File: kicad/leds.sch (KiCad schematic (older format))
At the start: 85 parts, among them U6 74HC154

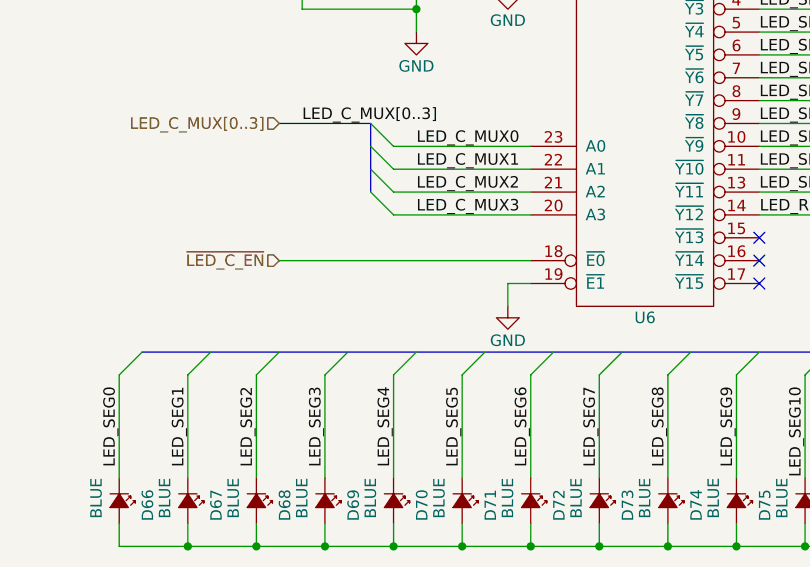
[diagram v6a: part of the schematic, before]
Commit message: Finished round two routing
This layout cuts through the middle of no planes and has more
predictable power paths (without needing Hyperlynx or something like
that). It also routes all signals but the LED-related ones on just the
top and bottom layers, as it is meant to be. It also nearly comforms to
the recommended layout for the regulator. There also aren't any ICs
without a full reference plane beneath them.

Basically, it's awesome.
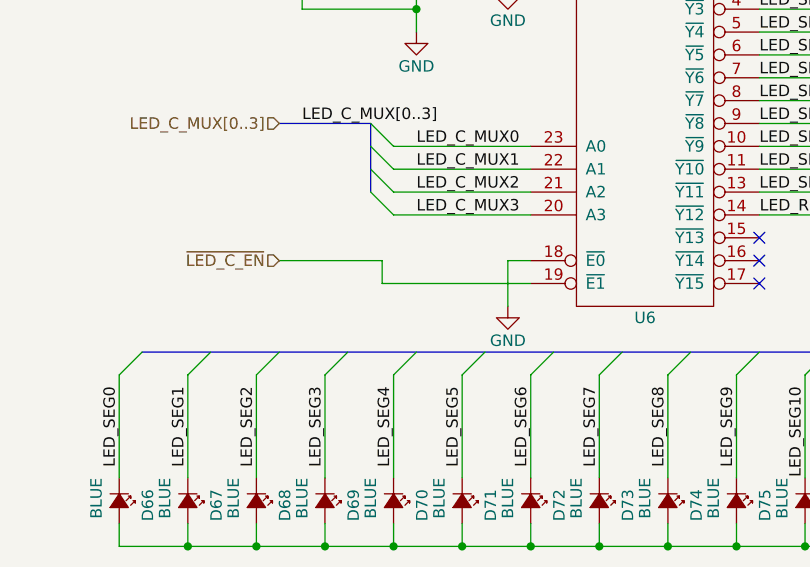
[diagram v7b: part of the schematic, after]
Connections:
- net GND: now also U6.18 (~E0); no longer U6.19 (~E1)
- net ~LED_C_EN: now also U6.19 (~E1); no longer U6.18 (~E0)
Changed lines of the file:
@@
 Text Label 4100 6200 2    50   ~ 0
 LED_RGB_C
-Wire Wire Line
-	1600 6400 2700 6400
 Wire Bus Line
 	1600 5800 2000 5800
@@
 	1700 5300 2200 5300
 Connection ~ 2200 5300
-Wire Wire Line
-	2600 6600 2600 6500
-Wire Wire Line
-	2600 6500 2700 6500
 Wire Wire Line
 	4600 1300 4600 1400
@@
 	1    0    0    -1
 $EndComp
+Wire Wire Line
+	2700 6400 2600 6400
+Wire Wire Line
+	2600 6400 2600 6600
+Wire Wire Line
+	2050 6500 2700 6500
+Wire Wire Line
+	2050 6500 2050 6400
+Wire Wire Line
+	2050 6400 1600 6400
 $EndSCHEMATC

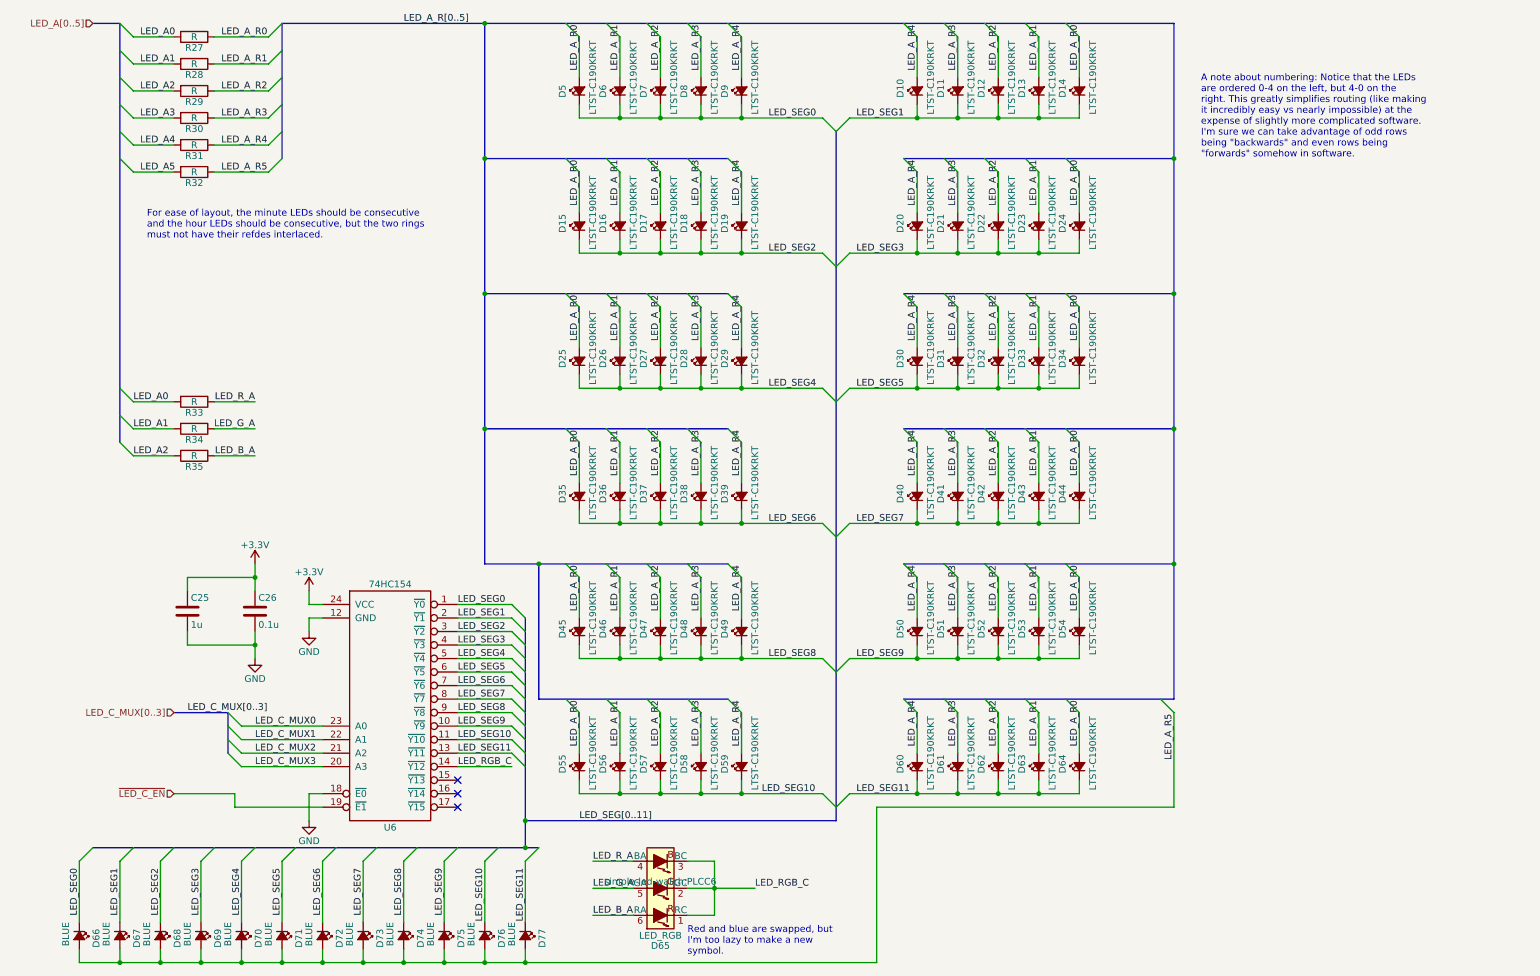
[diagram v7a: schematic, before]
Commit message: Changed out D65 RGB LED for a shorter 0606 part
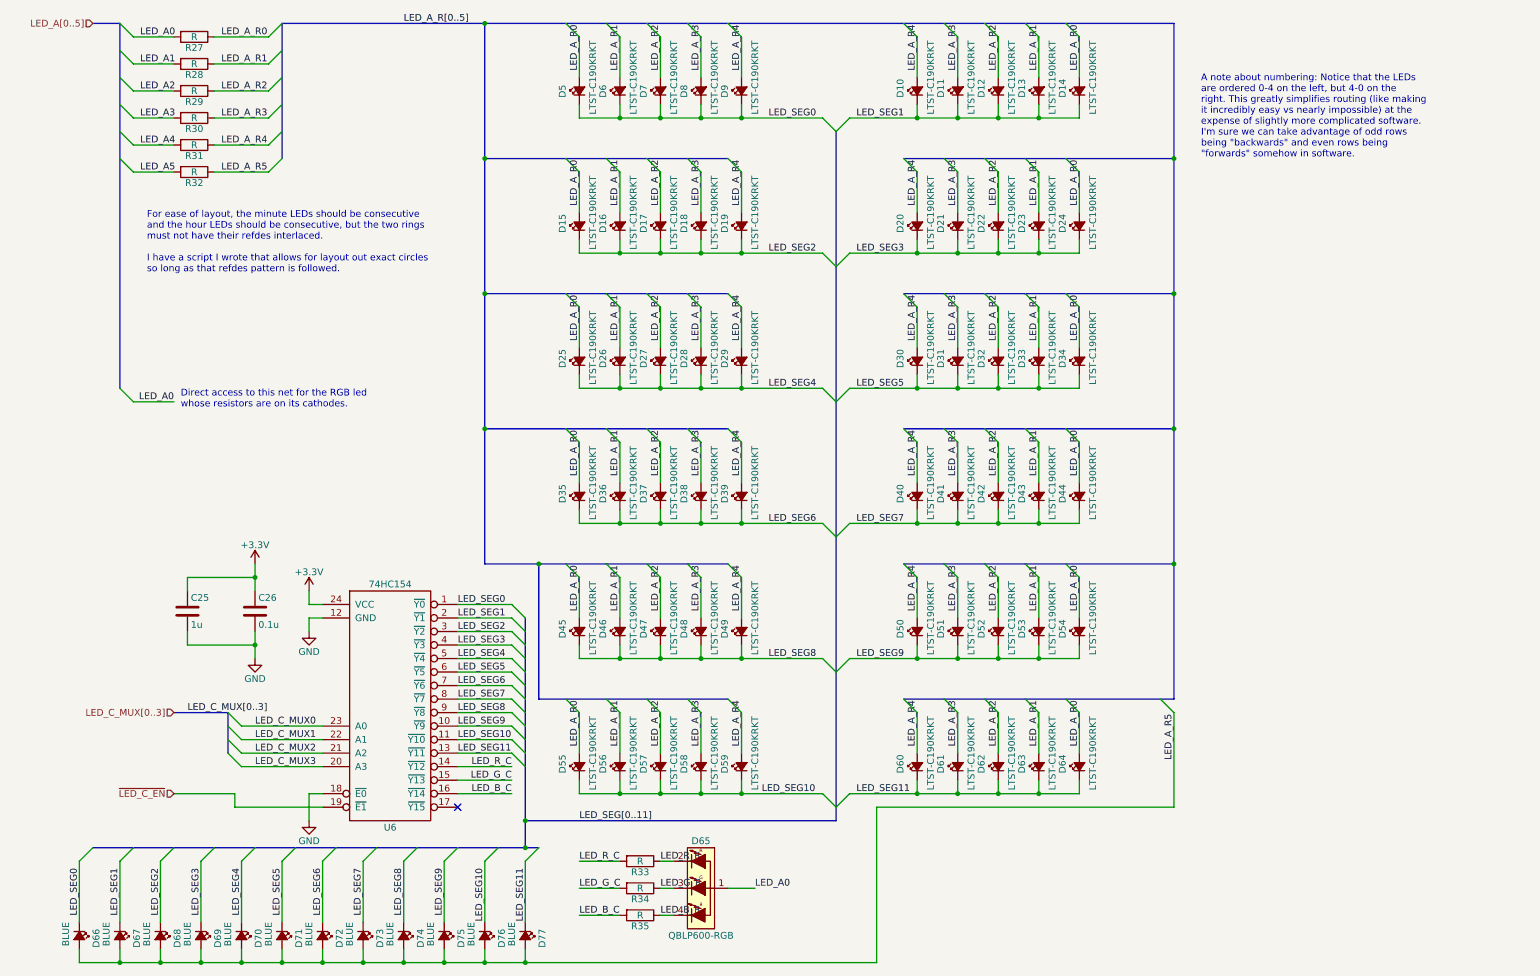
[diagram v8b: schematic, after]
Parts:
- removed D65: LED_RGB, simple-led-watch:PLCC6, symbol LED_RGB
- added D65: QBLP600-RGB, simple-led-watch:LED-0606, symbol Led_RGB_CA
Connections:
- net LED_A0: now also D65.1; no longer R33.2
- net LED_A1: no longer R34.2
- net LED_A2: no longer R35.2
- net LED_G_C: now reaches U6.15 (~Y13)
- net LED_G_C: now also R34.2
- net LED_B_C: now reaches U6.16 (~Y14)
- net LED_B_C: now also R35.2
- net LED_B_A renamed LED_B_R
- net LED_B_R: now also D65.4 (B)
- net LED_G_A renamed LED_G_R
- net LED_G_R: now also D65.3 (G)
- net LED_RGB_C renamed LED_R_C
- net LED_R_C: now also R33.2
- net LED_R_A renamed LED_R_R
- net LED_R_R: now also D65.2 (R)
- no-connect marks 3 -> 1
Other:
- note added: "Direct access to this net for the RGB led\nwhose resistors are on its cathodes."
- note added: "For ease of layout, the minute LEDs should be consecutive\nand the hour LEDs should be consecutive, but the two rings\nmust not have their refdes interlaced.\n\nI have a script I wrote that allows for layout out exact circles\nso long as that refdes pattern is followed."
- note removed: "For ease of layout, the minute LEDs should be consecutive\nand the hour LEDs should be consecutive, but the two rings\nmust not have their refdes interlaced."
- note removed: "Red and blue are swapped, but\nI'm too lazy to make a new\nsymbol."
- moved on the sheet: R33, R34, R35
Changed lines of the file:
@@
 Entry Wire Line
 	4200 6900 4300 6800
-Text Notes 1400 2300 0    50   ~ 0
-For ease of layout, the minute LEDs should be consecutive\nand the hour LEDs should be consecutive, but the two rings\nmust not have their refdes interlaced.
+Text Notes 1400 2550 0    50   ~ 0
+For ease of layout, the minute LEDs should be consecutive\nand the hour LEDs should be consecutive, but the two rings\nmust not have their refdes interlaced.\n\nI have a script I wrote that allows for layout out exact circles\nso long as that refdes pattern is followed.
 Entry Wire Line
 	8900 5700 9000 5800
@@
 Text Label 6650 6400 0    50   ~ 0
 LED_SEG11
-Text Label 4100 6200 2    50   ~ 0
-LED_RGB_C
 Wire Bus Line
 	1600 5800 2000 5800
@@
 	1000 700  1200 700
 Wire Bus Line
-	1200 700  1200 3800
-Wire Bus Line
 	2400 700  2400 1700
 Wire Wire Line
@@
 	9000 6500 6800 6500
 Connection ~ 4200 7650
-Wire Wire Line
-	3700 6200 4100 6200
-$Comp
-L LED_RGB D65
-U 1 1 5804CA95
-P 5200 7100
-F 0 "D65" H 5200 7525 50  0000 C CNN
-F 1 "LED_RGB" H 5200 7450 50  0000 C CNN
-F 2 "simple-led-watch:PLCC6" H 5200 7050 50  0000 C CNN
-F 3 "" H 5200 7050 50  0000 C CNN
-F 4 "CLY6D-FKC-CNP1ST1E1BB7D3D3CT-ND" H 5200 7100 60  0001 C CNN "Part No."
-	1    5200 7100
-	-1   0    0    1
-$EndComp
-Text Notes 5400 7600 0    50   ~ 0
-Red and blue are swapped, but\nI'm too lazy to make a new\nsymbol.
 $Comp
 L R R33
 U 1 1 5804E18D
-P 1750 3500
-F 0 "R33" V 1830 3500 50  0000 C CNN
-F 1 "R" V 1750 3500 50  0000 C CNN
-F 2 "Resistors_SMD:R_0402" V 1680 3500 50  0001 C CNN
-F 3 "" H 1750 3500 50  0000 C CNN
-	1    1750 3500
+P 5050 6900
+F 0 "R33" V 5130 6900 50  0000 C CNN
+F 1 "R" V 5050 6900 50  0000 C CNN
+F 2 "Resistors_SMD:R_0402" V 4980 6900 50  0001 C CNN
+F 3 "" H 5050 6900 50  0000 C CNN
+	1    5050 6900
 	0    1    1    0
 $EndComp
@@
 L R R34
 U 1 1 5804E381
-P 1750 3700
-F 0 "R34" V 1830 3700 50  0000 C CNN
-F 1 "R" V 1750 3700 50  0000 C CNN
-F 2 "Resistors_SMD:R_0402" V 1680 3700 50  0001 C CNN
-F 3 "" H 1750 3700 50  0000 C CNN
-	1    1750 3700
+P 5050 7100
+F 0 "R34" V 5130 7100 50  0000 C CNN
+F 1 "R" V 5050 7100 50  0000 C CNN
+F 2 "Resistors_SMD:R_0402" V 4980 7100 50  0001 C CNN
+F 3 "" H 5050 7100 50  0000 C CNN
+	1    5050 7100
 	0    1    1    0
 $EndComp
@@
 L R R35
 U 1 1 5804E495
-P 1750 3900
-F 0 "R35" V 1830 3900 50  0000 C CNN
-F 1 "R" V 1750 3900 50  0000 C CNN
-F 2 "Resistors_SMD:R_0402" V 1680 3900 50  0001 C CNN
-F 3 "" H 1750 3900 50  0000 C CNN
-	1    1750 3900
+P 5050 7300
+F 0 "R35" V 5130 7300 50  0000 C CNN
+F 1 "R" V 5050 7300 50  0000 C CNN
+F 2 "Resistors_SMD:R_0402" V 4980 7300 50  0001 C CNN
+F 3 "" H 5050 7300 50  0000 C CNN
+	1    5050 7300
 	0    1    1    0
 $EndComp
 Text Label 5900 7100 0    50   ~ 0
-LED_RGB_C
-Wire Wire Line
-	5400 7100 5900 7100
-Wire Wire Line
-	5600 6900 5600 7300
-Wire Wire Line
-	5600 6900 5400 6900
-Connection ~ 5600 7100
-Wire Wire Line
-	5600 7300 5400 7300
-Wire Wire Line
-	1900 3500 2200 3500
-Wire Wire Line
-	1900 3700 2200 3700
-Wire Wire Line
-	1900 3900 2200 3900
-Text Label 2200 3500 2    50   ~ 0
-LED_R_A
-Text Label 2200 3700 2    50   ~ 0
-LED_G_A
-Text Label 2200 3900 2    50   ~ 0
-LED_B_A
-Entry Wire Line
-	1200 3800 1300 3900
-Entry Wire Line
-	1200 3600 1300 3700
+LED_A0
 Entry Wire Line
 	1200 3400 1300 3500
 Wire Wire Line
 	1300 3500 1600 3500
-Wire Wire Line
-	1300 3700 1600 3700
-Wire Wire Line
-	1300 3900 1600 3900
-Text Label 1300 3500 0    50   ~ 0
+Text Label 1600 3500 2    50   ~ 0
 LED_A0
-Text Label 1300 3700 0    50   ~ 0
-LED_A1
-Text Label 1300 3900 0    50   ~ 0
-LED_A2
 Connection ~ 4200 6800
 Wire Wire Line
 	6800 6500 6800 7650
-Wire Wire Line
-	4700 6900 5000 6900
-Wire Wire Line
-	4700 7100 5000 7100
-Wire Wire Line
-	4700 7300 5000 7300
-Text Label 4700 6900 0    50   ~ 0
-LED_R_A
-Text Label 4700 7100 0    50   ~ 0
-LED_G_A
-Text Label 4700 7300 0    50   ~ 0
-LED_B_A
-NoConn ~ 3700 6300
-NoConn ~ 3700 6400
 NoConn ~ 3700 6500
 Text Notes 9200 1700 0    50   ~ 0
@@
 Wire Wire Line
 	2050 6400 1600 6400
+$Comp
+L Led_RGB_CA D65
+U 1 1 5844C5B1
+P 5500 7100
+F 0 "D65" H 5500 7450 50  0000 C CNN
+F 1 "QBLP600-RGB" H 5500 6750 50  0000 C CNN
+F 2 "simple-led-watch:LED-0606" H 5455 7050 50  0001 C CNN
+F 3 "" H 5455 7050 50  0000 C CNN
+F 4 "1516-1184-1-ND" H 5500 7100 60  0001 C CNN "Part No."
+	1    5500 7100
+	1    0    0    -1
+$EndComp
+Text Label 4100 6200 2    50   ~ 0
+LED_R_C
+Wire Wire Line
+	3700 6200 4100 6200
+Wire Wire Line
+	3700 6300 4100 6300
+Wire Wire Line
+	3700 6400 4100 6400
+Text Label 4100 6300 2    50   ~ 0
+LED_G_C
+Text Label 4100 6400 2    50   ~ 0
+LED_B_C
+Wire Bus Line
+	1200 700  1200 3400
+Text Label 4600 7300 0    50   ~ 0
+LED_B_C
+Text Label 4600 6900 0    50   ~ 0
+LED_R_C
+Text Label 4600 7100 0    50   ~ 0
+LED_G_C
+Wire Wire Line
+	4600 6900 4900 6900
+Wire Wire Line
+	4600 7100 4900 7100
+Wire Wire Line
+	4600 7300 4900 7300
+Text Notes 1650 3550 0    50   ~ 0
+Direct access to this net for the RGB led\nwhose resistors are on its cathodes.
+Wire Wire Line
+	5900 7100 5700 7100
+Wire Wire Line
+	5300 6900 5200 6900
+Wire Wire Line
+	5300 7100 5200 7100
+Wire Wire Line
+	5300 7300 5200 7300
+Text Label 5200 6900 0    50   ~ 0
+LED_R_R
+Text Label 5200 7100 0    50   ~ 0
+LED_G_R
+Text Label 5200 7300 0    50   ~ 0
+LED_B_R
 $EndSCHEMATC
